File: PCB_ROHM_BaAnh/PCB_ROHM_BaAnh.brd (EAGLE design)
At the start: 185.5 x 146.5 mm, 185 parts, among them IC1 TXB0108PWR, IC2 TXB0108PWR, IC3 TPS76201DBVR, IC4 TXB0108PWR, IC5 TPS76201DBVR, IC6 TXB0108PWR, IC7 TPS76201DBVR, Q1 BSH103,235, Q10 BSH103,235, Q11 BSH103,235, Q12 BSH103,235, Q13 BSH103,235, Q14 BSH103,235, Q15 BSH103,235, Q16 BSH103,235, Q17 BSH103,235, Q18 BSH103,235, Q19 BSH103,235, Q2 BSH103,235, Q20 BSH103,235, Q21 BSH103,235, Q3 BSH103,235, Q4 BSH103,235, Q5 BSH103,235, Q6 BSH103,235, Q7 BSH103,235, Q8 BSH103,235, Q9 BSH103,235

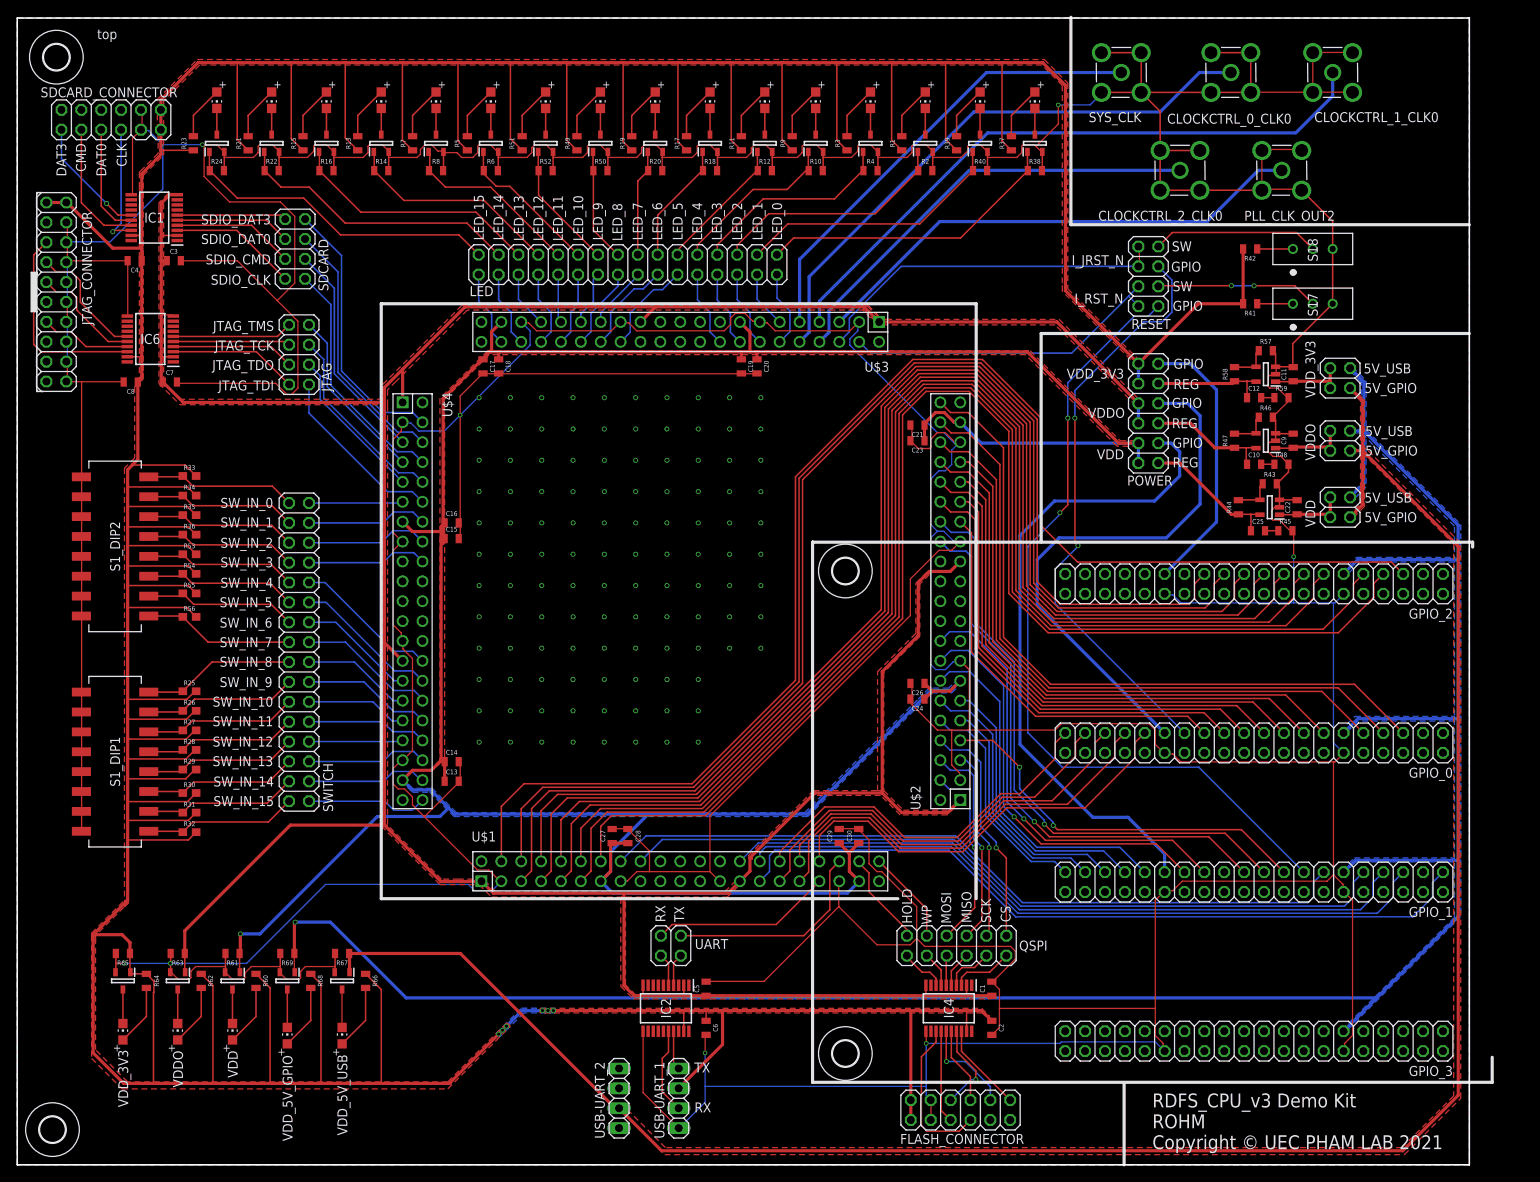
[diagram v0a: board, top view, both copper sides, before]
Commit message: Update PCB of Dao, change switch resistor to 0805
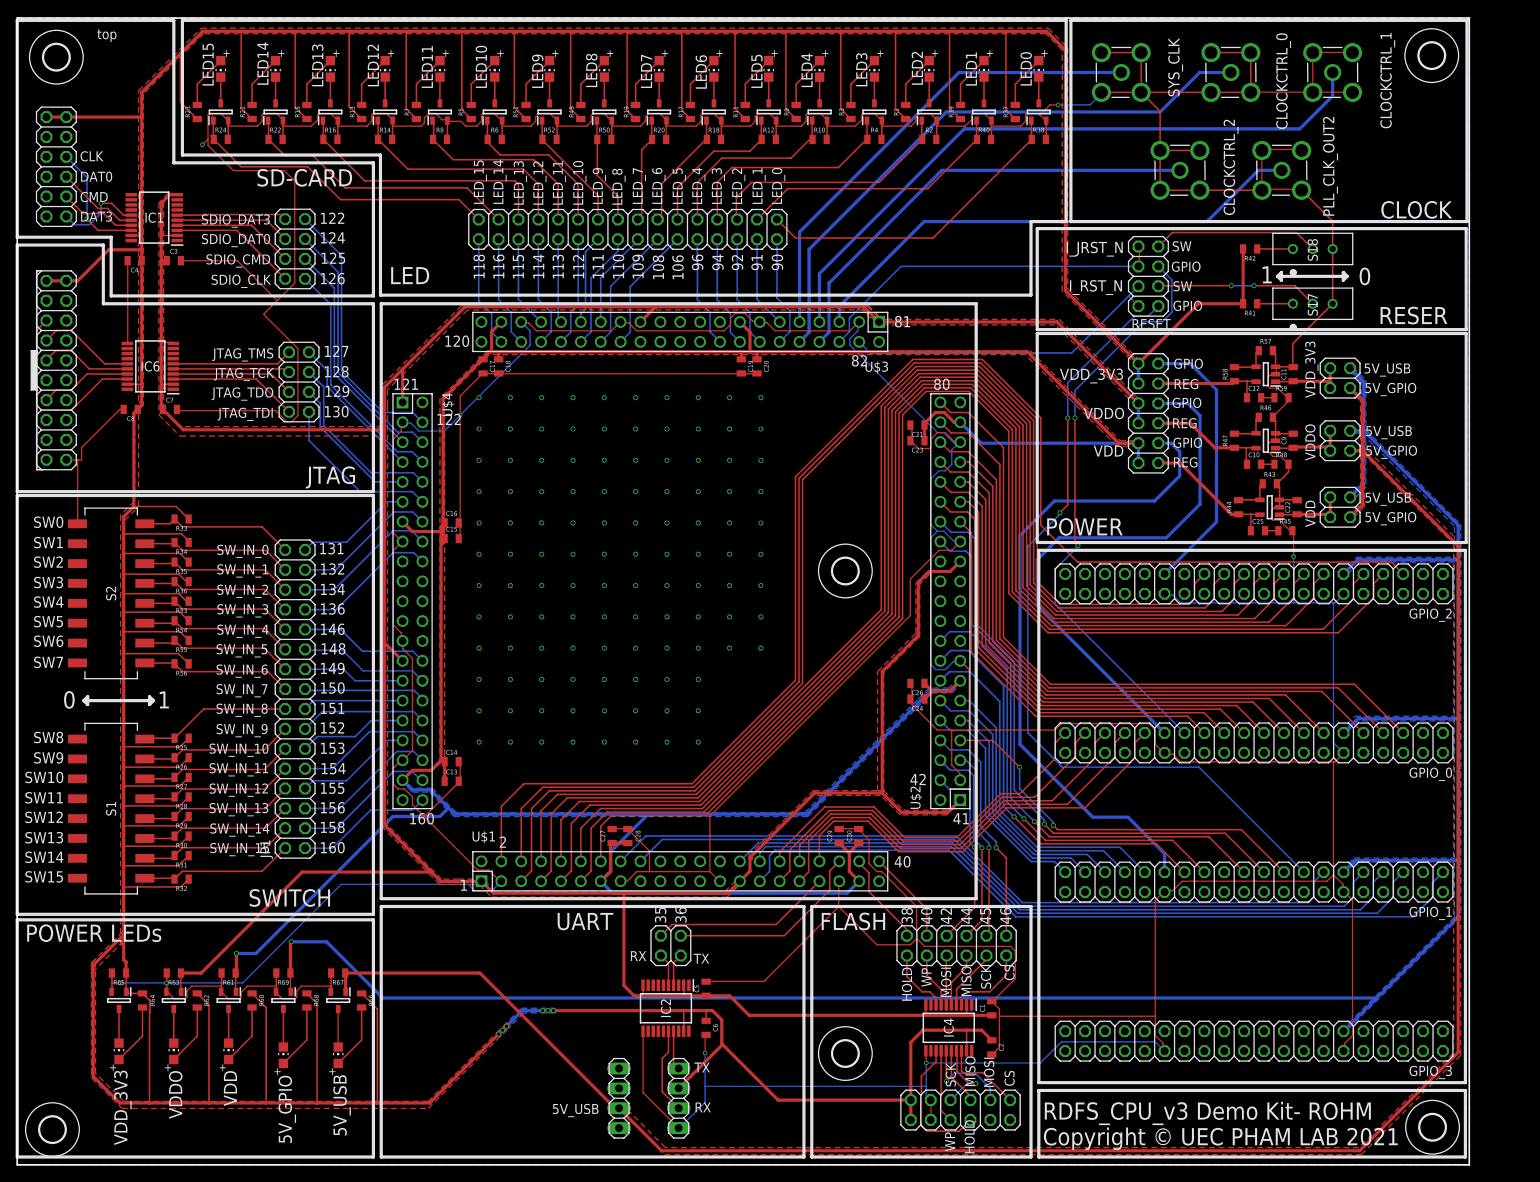
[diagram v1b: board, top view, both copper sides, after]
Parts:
- removed S1_DIP1, S1_DIP2: 219-8LPST, SamacSys_Parts:2198LPST
- removed SWITCH: (no value), pinhead:2X16
- added H5, H6: MOUNT-HOLE3.3, holes:3,3
- added JP1: (no value), pinhead:2X16
- added S1, S2: 219-8LPST, SamacSys_Parts:2198LPST
- R25, R26, R27, R28, R29, R30, R31, R32, R33, R34, R35, R36, R53, R54, R55, R56: device SparkFun-Resistors:0603 -> SparkFun-Resistors:0805
- moved JTAG_CONNECTOR 10.0 mm to (-78.0, 29.5)
- moved SDCARD_CONNECTOR 9.22 mm to (-78.0, 55.5), turned to 270 degrees
- moved R25 6.08 mm to (-62.0, -17.5), turned to 180 degrees
- moved R26 6.08 mm to (-62.0, -20.0), turned to 180 degrees
- moved R27 6.08 mm to (-62.0, -22.5), turned to 180 degrees
- moved R28 6.08 mm to (-62.0, -25.0), turned to 180 degrees
- moved R29 6.08 mm to (-62.0, -27.5), turned to 180 degrees
- moved R32 6.08 mm to (-62.0, -35.5), turned to 180 degrees
- moved R34 6.08 mm to (-62.0, 7.50), turned to 180 degrees
- moved R35 6.08 mm to (-62.0, 5.00), turned to 180 degrees
- moved R36 6.08 mm to (-62.0, 2.50), turned to 180 degrees
- moved R53 6.08 mm to (-62.0, 0.00), turned to 180 degrees
- moved R54 6.08 mm to (-62.0, -2.50), turned to 180 degrees
- moved R55 6.08 mm to (-62.0, -5.00), turned to 180 degrees
- moved R56 6.08 mm to (-62.0, -8.00), turned to 180 degrees
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- renumbered CLOCKCTRL_0_CLK0 to CLOCKCTRL_0, CLOCKCTRL_1_CLK0 to CLOCKCTRL_1, CLOCKCTRL_2_CLK0 to CLOCKCTRL_2
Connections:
- net GND: now also S1.10, S1.11, S1.12, S1.13, S1.14, S1.15, S1.16, S1.9, S2.10, S2.11, S2.12, S2.13, S2.14, S2.15, S2.16, S2.9; no longer S1_DIP1.10, S1_DIP1.11, S1_DIP1.12, S1_DIP1.13, S1_DIP1.14, S1_DIP1.15, S1_DIP1.16, S1_DIP1.9, S1_DIP2.10, S1_DIP2.11, S1_DIP2.12, S1_DIP2.13, S1_DIP2.14, S1_DIP2.15, S1_DIP2.16, S1_DIP2.9
- net GPIO_IN[0]: now also JP1.31; no longer SWITCH.31
- net GPIO_IN[10]: now also JP1.11; no longer SWITCH.11
- net GPIO_IN[11]: now also JP1.9; no longer SWITCH.9
- net GPIO_IN[12]: now also JP1.7; no longer SWITCH.7
- net GPIO_IN[13]: now also JP1.5; no longer SWITCH.5
- net GPIO_IN[14]: now also JP1.3; no longer SWITCH.3
- net GPIO_IN[15]: now also JP1.1; no longer SWITCH.1
- net GPIO_IN[1]: now also JP1.29; no longer SWITCH.29
- net GPIO_IN[2]: now also JP1.27; no longer SWITCH.27
- net GPIO_IN[3]: now also JP1.25; no longer SWITCH.25
- net GPIO_IN[4]: now also JP1.23; no longer SWITCH.23
- net GPIO_IN[5]: now also JP1.21; no longer SWITCH.21
- net GPIO_IN[6]: now also JP1.19; no longer SWITCH.19
- net GPIO_IN[7]: now also JP1.17; no longer SWITCH.17
- net GPIO_IN[8]: now also JP1.15; no longer SWITCH.15
- net GPIO_IN[9]: now also JP1.13; no longer SWITCH.13
- net N$48: now also JP1.32, R33.2, S2.8; no longer R31.1, S1_DIP1.2, SWITCH.4
- net N$49: now also JP1.30, R34.2, S2.7; no longer R30.1, S1_DIP1.3, SWITCH.6
- net N$50: now also JP1.28, R35.2, S2.6; no longer R29.1, S1_DIP1.4, SWITCH.8
- net N$51: now also JP1.26, R36.2, S2.5; no longer R28.1, S1_DIP1.5, SWITCH.10
- net N$56: now also JP1.24, R53.2, S2.4; no longer R27.1, S1_DIP1.6, SWITCH.12
- net N$57: now also JP1.22, R54.2, S2.3; no longer R26.1, S1_DIP1.7, SWITCH.14
- net N$58: now also JP1.20, R55.2, S2.2; no longer R25.1, S1_DIP1.8, SWITCH.16
- net N$60: now also JP1.18, R56.2, S2.1; no longer R32.1, S1_DIP1.1, SWITCH.2
- net N$66: now also JP1.16, R25.2, S1.8; no longer R55.1, S1_DIP2.2, SWITCH.20
- net N$67: now also JP1.14, R26.2, S1.7; no longer R54.1, S1_DIP2.3, SWITCH.22
- net N$68: now also JP1.12, R27.2, S1.6; no longer R53.1, S1_DIP2.4, SWITCH.24
- net N$69: now also JP1.10, R28.2, S1.5; no longer R36.1, S1_DIP2.5, SWITCH.26
- net N$72: now also JP1.8, R29.2, S1.4; no longer R35.1, S1_DIP2.6, SWITCH.28
- net N$73: now also JP1.6, R30.2, S1.3; no longer R34.1, S1_DIP2.7, SWITCH.30
- net N$74: now also JP1.4, R31.2, S1.2; no longer R33.1, S1_DIP2.8, SWITCH.32
- net N$75: now also JP1.2, R32.2, S1.1; no longer R56.1, S1_DIP2.1, SWITCH.18
- net VDD_3V3: now also R25.1, R26.1, R27.1, R28.1, R29.1, R30.1, R31.1, R32.1, R33.1, R34.1, R35.1, R36.1, R53.1, R54.1, R55.1, R56.1; no longer R25.2, R26.2, R27.2, R28.2, R29.2, R30.2, R31.2, R32.2, R33.2, R34.2, R35.2, R36.2, R53.2, R54.2, R55.2, R56.2
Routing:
- net GND: track 1441.8 -> 1337.6 mm
- net VDD_3V3: track 895.3 -> 913.3 mm
- net VDDO: track 457.1 -> 464.9 mm
- net SD_CMD: track 16.9 -> 9.81 mm
- net GPIO_OUT[11]: track 6.20 -> 10.7 mm
- net GPIO_OUT[9]: track 6.97 -> 11.5 mm
- net GPIO_OUT[8]: track 10.6 -> 15.1 mm
- net GPIO_OUT[7]: track 8.02 -> 12.5 mm
- net GPIO_OUT[4]: track 9.80 -> 14.3 mm
- net GPIO_OUT[3]: track 9.80 -> 14.3 mm
- net GPIO_OUT[2]: track 9.80 -> 14.3 mm
- net GPIO_OUT[1]: track 7.26 -> 11.8 mm
- net GPIO_OUT[15]: track 9.80 -> 14.3 mm
- net GPIO_OUT[13]: track 7.26 -> 11.8 mm
- net GPIO_OUT[12]: track 9.81 -> 14.3 mm
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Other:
- board text added: "0"
- board text added: "1"
- board text added: "106"
- board text added: "108"
- board text added: "109"
- board text added: "110"
- board text added: "111"
- board text added: "112"
- board text added: "113"
- board text added: "114"
- board text added: "115"
- board text added: "116"
- board text added: "118"
- board text added: "120"
- board text added: "121"
- board text added: "122"
- board text added: "124"
- board text added: "125"
- board text added: "126"
- board text added: "127"
- board text added: "128"
- board text added: "129"
- board text added: "130"
- board text added: "131"
- board text added: "132"
- board text added: "134"
- board text added: "136"
- board text added: "146"
- board text added: "148"
- board text added: "149"
- board text added: "150"
- board text added: "151"
- board text added: "152"
- board text added: "153"
- board text added: "154"
- board text added: "155"
- board text added: "156"
- board text added: "158"
- board text added: "160"
- board text added: "2"
- board text added: "35"
- board text added: "36"
- board text added: "38"
- board text added: "40"
- board text added: "41"
- board text added: "42"
- board text added: "44"
- board text added: "45"
- board text added: "46"
- board text added: "80"
- board text added: "81"
- board text added: "82"
- board text added: "90"
- board text added: "91"
- board text added: "92"
- board text added: "94"
- board text added: "96"
- board text added: "CLOCK"
- board text added: "FLASH"
- board text added: "JTAG"
- board text added: "LED"
- board text added: "LED0"
- board text added: "LED1"
- board text added: "LED10"
- board text added: "LED11"
- board text added: "LED12"
- board text added: "LED13"
- board text added: "LED14"
- board text added: "LED15"
- board text added: "LED2"
- board text added: "LED3"
- board text added: "LED4"
- board text added: "LED5"
- board text added: "LED6"
- board text added: "LED7"
- board text added: "LED8"
- board text added: "LED9"
- board text added: "POWER"
- board text added: "POWER LEDs"
- board text added: "RDFS_CPU_v3 Demo Kit- ROHM Copyright © UEC PHAM LAB 2021"
- board text added: "RESER"
- board text added: "SD-CARD"
- board text added: "SW0"
- board text added: "SW1"
- board text added: "SW10"
- board text added: "SW11"
- board text added: "SW12"
- board text added: "SW13"
- board text added: "SW14"
- board text added: "SW15"
- board text added: "SW2"
- board text added: "SW3"
- board text added: "SW4"
- board text added: "SW5"
- board text added: "SW6"
- board text added: "SW7"
- board text added: "SW8"
- board text added: "SW9"
- board text added: "SWITCH"
- board text added: "UART"
- board text removed: "RDFS_CPU_v3 Demo Kit ROHM Copyright © UEC PHAM LAB 2021"
- board text removed: "VDD_5V_GPIO"
- board text removed: "VDD_5V_USB"
